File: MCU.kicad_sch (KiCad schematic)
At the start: 16 parts, among them J3 Conn_01x06, J7 USB4110GFA, SW3 SW_Push, SW4 SW_Push, SW5 SW_Push, SW6 SW_Push, SW7 SW_Push, U3 NORA-B106-00B, U7 FAN5622SX, U8 ESDR0502NMUTBG, X1 Q13FC1350000400, X608 Display

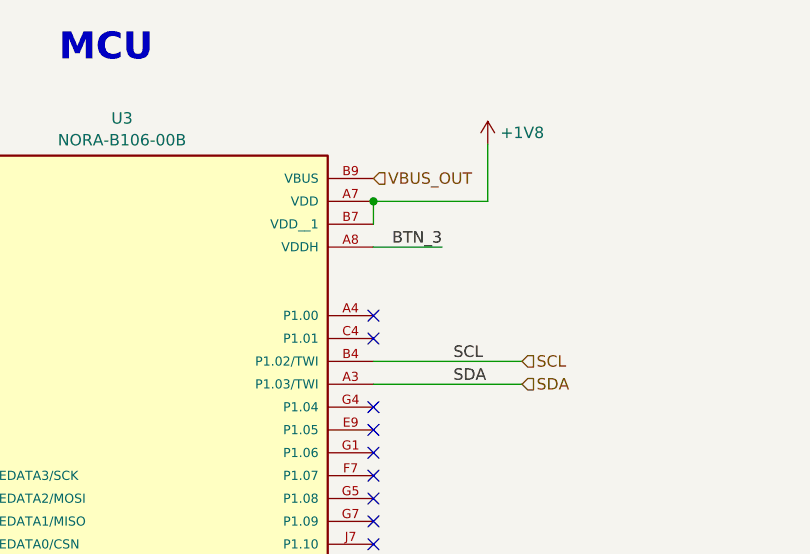
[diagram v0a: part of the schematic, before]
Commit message: New Case Files + Updated DRC Errors
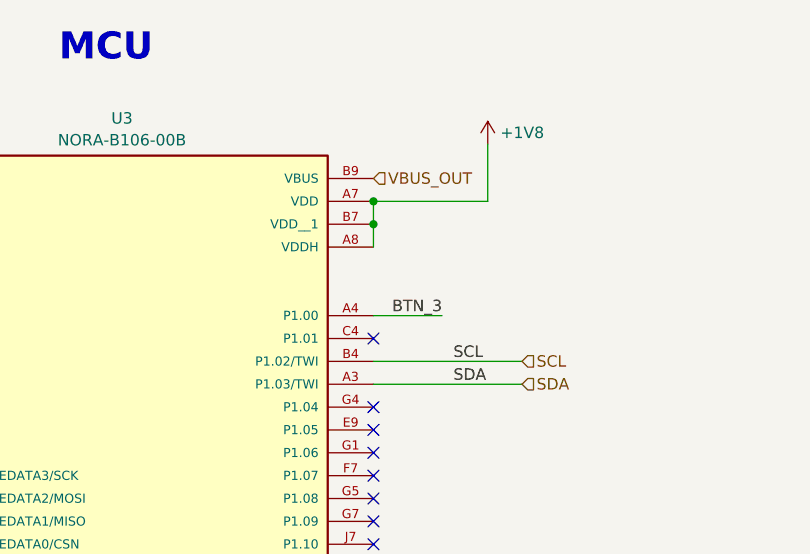
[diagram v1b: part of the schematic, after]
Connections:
- net +1V8: now also U3.A8 (VDDH)
- net BTN_3: now also U3.A4 (P1.00); no longer U3.A8 (VDDH)
- no-connect marks 18 -> 17
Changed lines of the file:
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@@
+	)
+	(junction
+		(at 172.72 35.56)
+		(diameter 0)
+		(color 0 0 0 0)
 	)
 	(junction
@@
 	)
 	(no_connect
-		(at 172.72 45.72)
-	)
-	(no_connect
 		(at 116.84 91.44)
 	)
@@
 	(wire
 		(pts
+			(xy 172.72 35.56) (xy 172.72 38.1)
+		)
+		(stroke
+			(width 0)
+			(type default)
+		)
+	)
+	(wire
+		(pts
 			(xy 100.33 109.22) (xy 116.84 109.22)
 		)
@@
 	(wire
 		(pts
+			(xy 180.34 45.72) (xy 172.72 45.72)
+		)
+		(stroke
+			(width 0)
+			(type default)
+		)
+	)
+	(wire
+		(pts
 			(xy 36.83 172.72) (xy 30.48 172.72)
 		)
@@
 		(pts
 			(xy 172.72 165.1) (xy 172.72 167.64)
-		)
-		(stroke
-			(width 0)
-			(type default)
-		)
-	)
-	(wire
-		(pts
-			(xy 180.34 38.1) (xy 172.72 38.1)
 		)
 		(stroke
@@
 		)
 	)
+	(label "BTN_3"
+		(at 180.34 45.72 180)
+		(effects
+			(font
+				(size 1.27 1.27)
+			)
+			(justify right bottom)
+		)
+	)
 	(label "SWO"
 		(at 102.87 119.38 0)
@@
 		(effects
 			(font
-				(size 1.27 1.27)
-			)
-			(justify right bottom)
-		)
-	)
-	(label "BTN_3"
-		(at 180.34 38.1 180)
-		(effects
-			(font

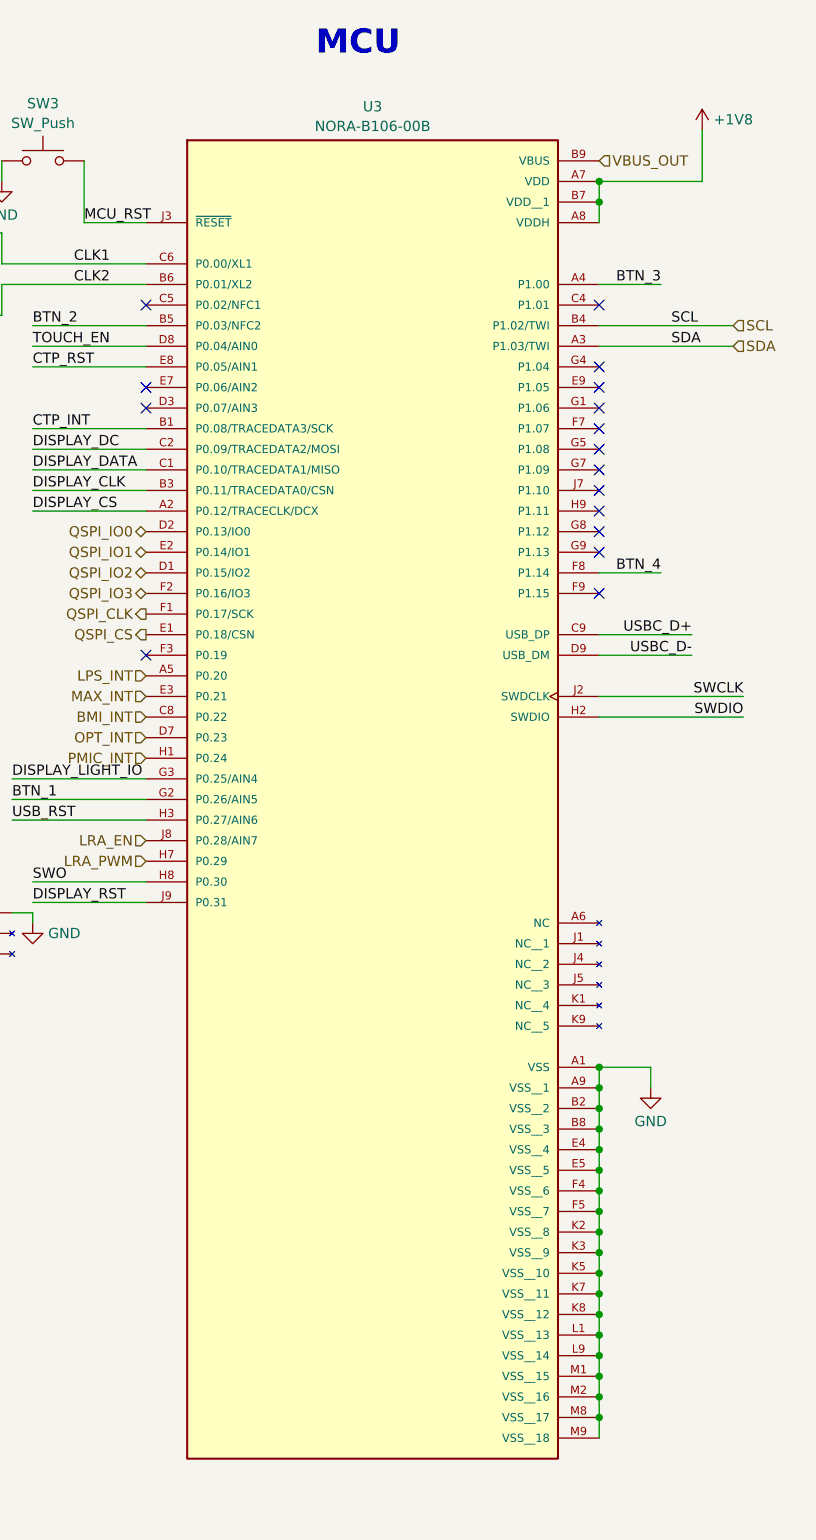
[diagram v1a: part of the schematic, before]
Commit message: Replaced b106 w b206 for jlc compatibility
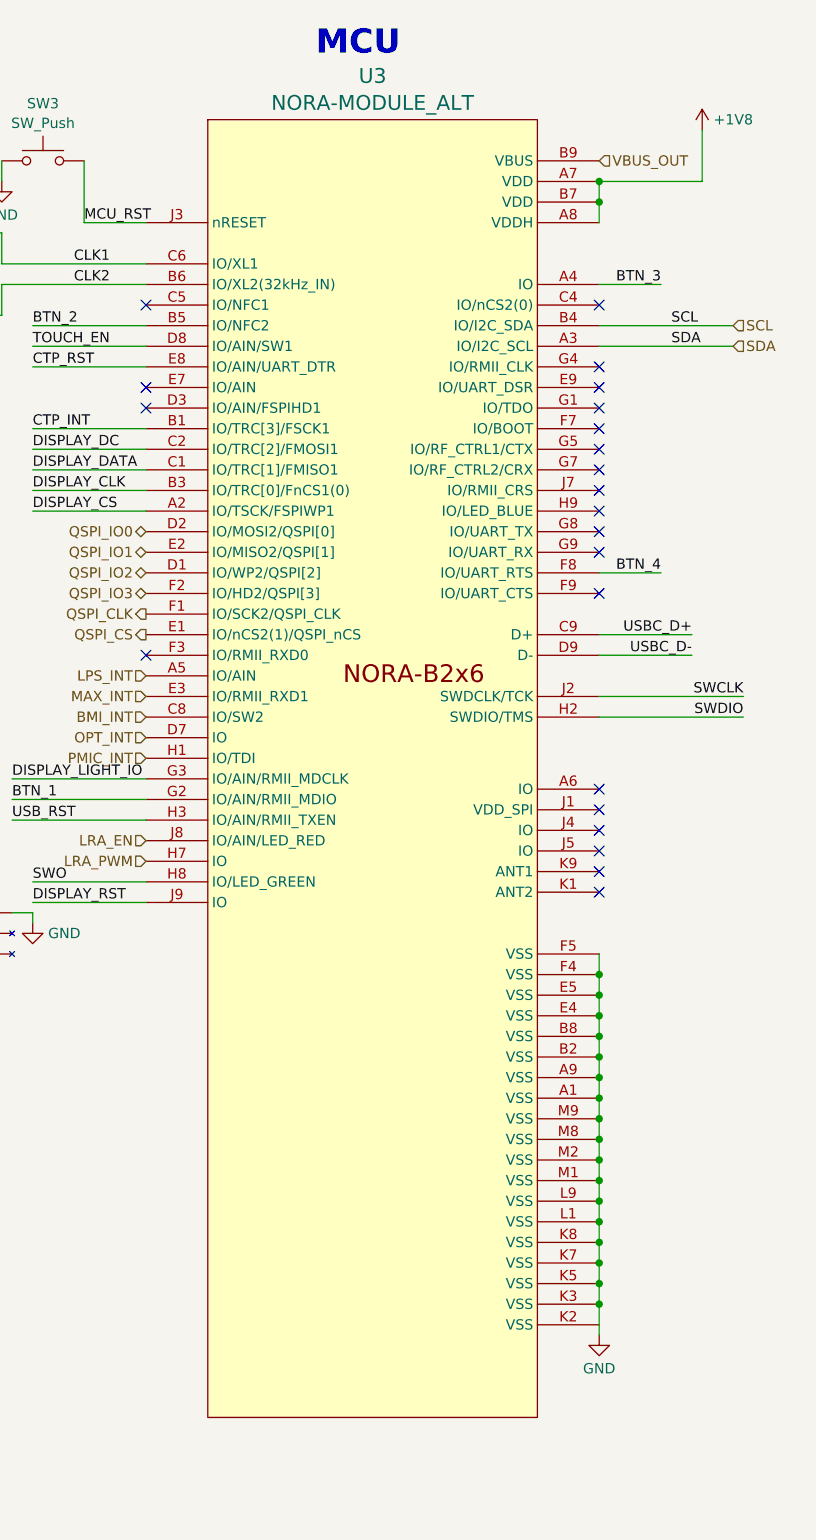
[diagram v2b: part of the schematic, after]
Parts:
- removed U3: NORA-B106-00B, Smart_Watch:XCVR_NORA-B106-00B, symbol Smart_Watch:NORA-B106-00B
- added U3: NORA-MODULE_ALT, ubloxLib:NORA_LGA82R_1430X1040X190_ANT, symbol Smart_Watch:NORA-B2x6
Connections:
- net +1V8: now also U3.A7 (VDD), U3.A8 (VDDH), U3.B7 (VDD)
- net BMI_INT: now also U3.C8 (IO/SW2)
- net BTN_1: now also U3.G2 (IO/AIN/RMII_MDIO)
- net BTN_2: now also U3.B5 (IO/NFC2)
- net BTN_3: now also U3.A4 (IO)
- net BTN_4: now also U3.F8 (IO/UART_RTS)
- net CLK1: now also U3.C6 (IO/XL1)
- net CLK2: now also U3.B6 (IO/XL2(32kHz_IN))
- net CTP_INT: now also U3.B1 (IO/TRC[3]/FSCK1)
- net CTP_RST: now also U3.E8 (IO/AIN/UART_DTR)
- net DISPLAY_CLK: now also U3.B3 (IO/TRC[0]/FnCS1(0))
- net DISPLAY_CS: now also U3.A2 (IO/TSCK/FSPIWP1)
- net DISPLAY_DATA: now also U3.C1 (IO/TRC[1]/FMISO1)
- net DISPLAY_DC: now also U3.C2 (IO/TRC[2]/FMOSI1)
- net DISPLAY_LIGHT_IO: now also U3.G3 (IO/AIN/RMII_MDCLK)
- net DISPLAY_RST: now also U3.J9 (IO)
- net GND: now also U3.A1 (VSS), U3.A9 (VSS), U3.B2 (VSS), U3.B8 (VSS), U3.E4 (VSS), U3.E5 (VSS), U3.F4 (VSS), U3.F5 (VSS), U3.K3 (VSS), U3.K5 (VSS), U3.K7 (VSS), U3.K8 (VSS), U3.L1 (VSS), U3.L9 (VSS), U3.M1 (VSS), U3.M2 (VSS), U3.M8 (VSS), U3.M9 (VSS)
- net LPS_INT: now also U3.A5 (IO/AIN)
- net LRA_EN: now also U3.J8 (IO/AIN/LED_RED)
- net LRA_PWM: now also U3.H7 (IO)
- net MAX_INT: now also U3.E3 (IO/RMII_RXD1)
- net MCU_RST: now also U3.J3 (nRESET)
- net OPT_INT: now also U3.D7 (IO)
- net PMIC_INT: now also U3.H1 (IO/TDI)
- net QSPI_CLK: now also U3.F1 (IO/SCK2/QSPI_CLK)
- net QSPI_CS: now also U3.E1 (IO/nCS2(1)/QSPI_nCS)
- net QSPI_IO0: now also U3.D2 (IO/MOSI2/QSPI[0])
- net QSPI_IO1: now also U3.E2 (IO/MISO2/QSPI[1])
- net QSPI_IO2: now also U3.D1 (IO/WP2/QSPI[2])
- net QSPI_IO3: now also U3.F2 (IO/HD2/QSPI[3])
- net SCL: now also U3.B4 (IO/I2C_SDA)
- net SDA: now also U3.A3 (IO/I2C_SCL)
- net SWCLK: now also U3.J2 (SWDCLK/TCK)
- net SWDIO: now also U3.H2 (SWDIO/TMS)
- net SWO: now also U3.H8 (IO/LED_GREEN)
- net TOUCH_EN: now also U3.D8 (IO/AIN/SW1)
- net USBC_D+: now also U3.C9 (D+)
- net USBC_D-: now also U3.D9 (D-)
- net USB_RST: now also U3.H3 (IO/AIN/RMII_TXEN)
- net VBUS_OUT: now also U3.B9 (VBUS)
- no-connect marks 17 -> 23

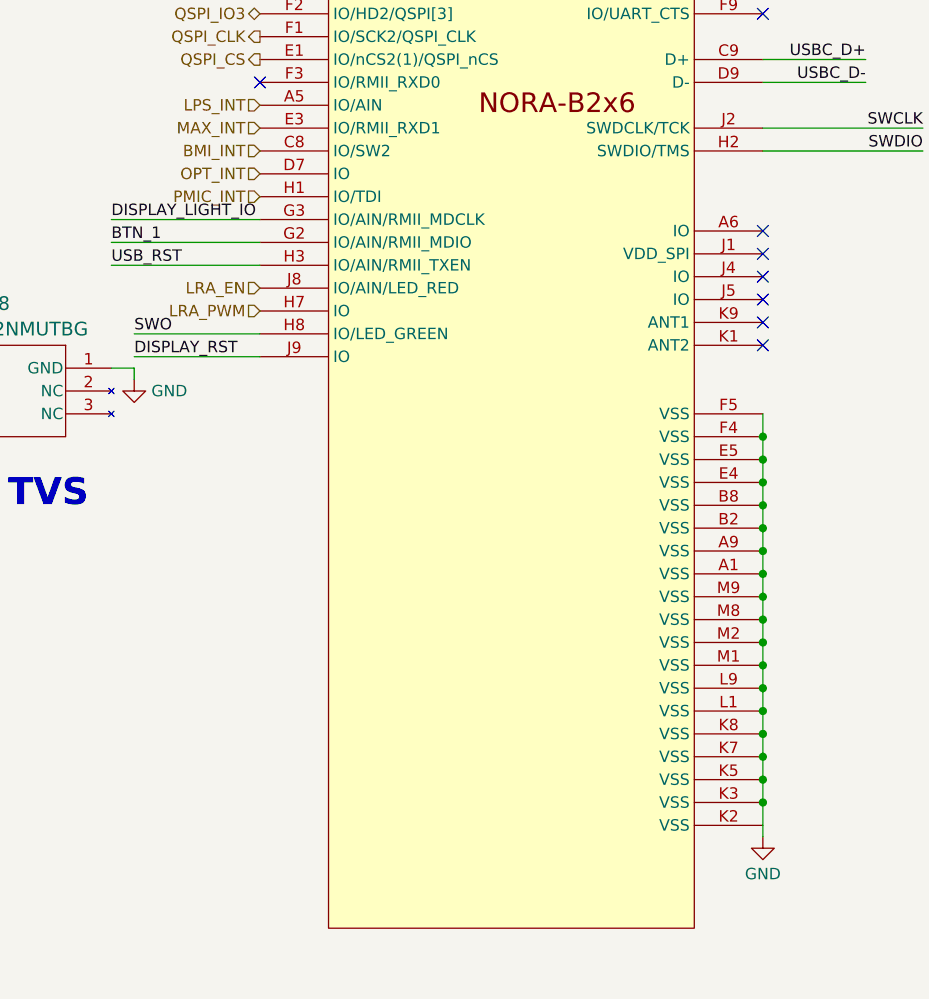
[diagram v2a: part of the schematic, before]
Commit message: Removed amb light, extended board for usbc and buttons
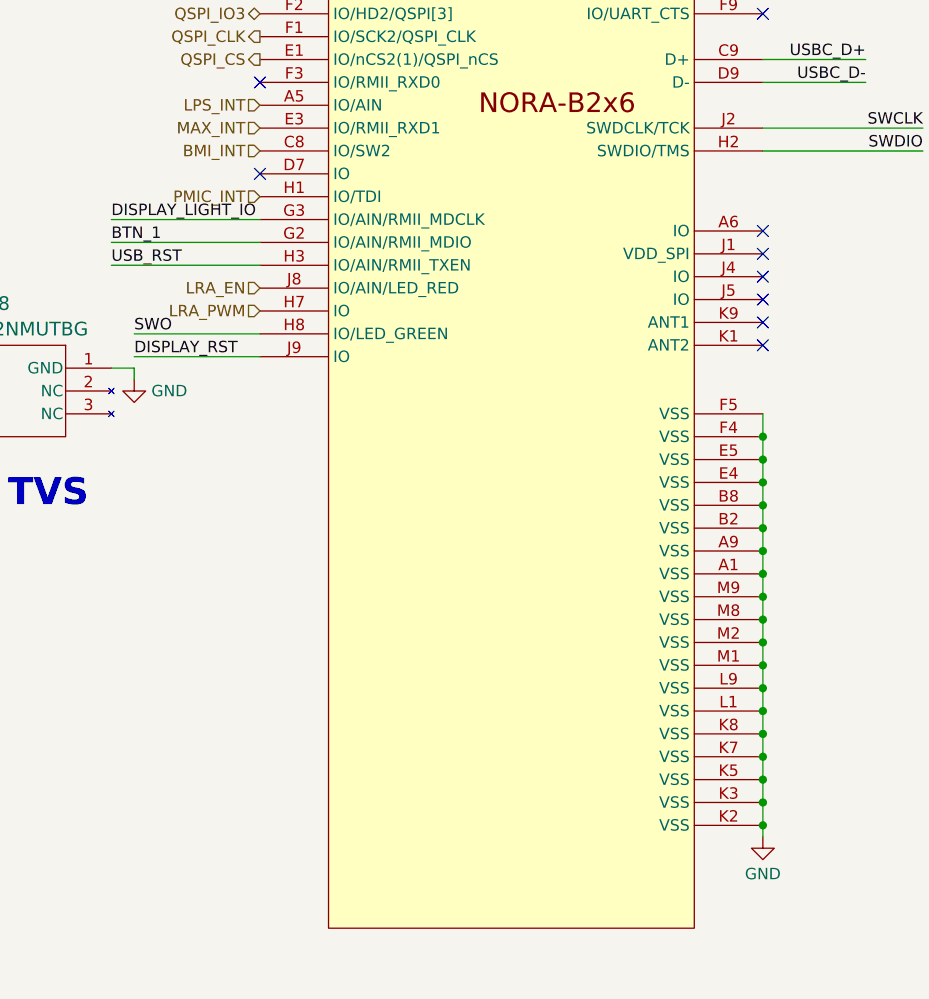
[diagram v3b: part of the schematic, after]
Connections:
- net GND: now also U3.K2 (VSS)
- net OPT_INT: no longer names the net of U3.D7 (IO)
- no-connect marks 23 -> 24
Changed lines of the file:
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@@
+	)
+	(junction
+		(at 172.72 173.99)
+		(diameter 0)
+		(color 0 0 0 0)
 	)
 	(junction
@@
 	)
 	(no_connect
+		(at 116.84 101.6)
+	)
+	(no_connect
 		(at 172.72 115.57)
 	)
@@
 	(wire
 		(pts
+			(xy 172.72 173.99) (xy 172.72 175.26)
+		)
+		(stroke
+			(width 0)
+			(type default)
+		)
+	)
+	(wire
+		(pts
 			(xy 13.97 114.3) (xy 22.86 114.3)
 		)
@@
 	(wire
 		(pts
-			(xy 172.72 140.97) (xy 172.72 175.26)
+			(xy 172.72 140.97) (xy 172.72 173.99)
 		)
 		(stroke
@@
 		(effects
 			(font
-				(size 1.27 1.27)
-			)
-			(justify right)
-		)
-	)
-	(hierarchical_label "OPT_INT"
-		(shape input)
-		(at 116.84 101.6 180)
-		(effects
-			(font
